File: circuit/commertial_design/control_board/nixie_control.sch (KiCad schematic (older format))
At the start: 34 parts, among them IC1 ATMEGA328P-A, P1 CONN_01X08, P2 CONN_02X03, P3 CONN_01X12, P4 CONN_01X04, P5 BLUETOOTH_SJ, P6 CONN_02X03, Q3 Q_NPN_EBC, Q4 Q_NPN_EBC, SW1 SW_PUSH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

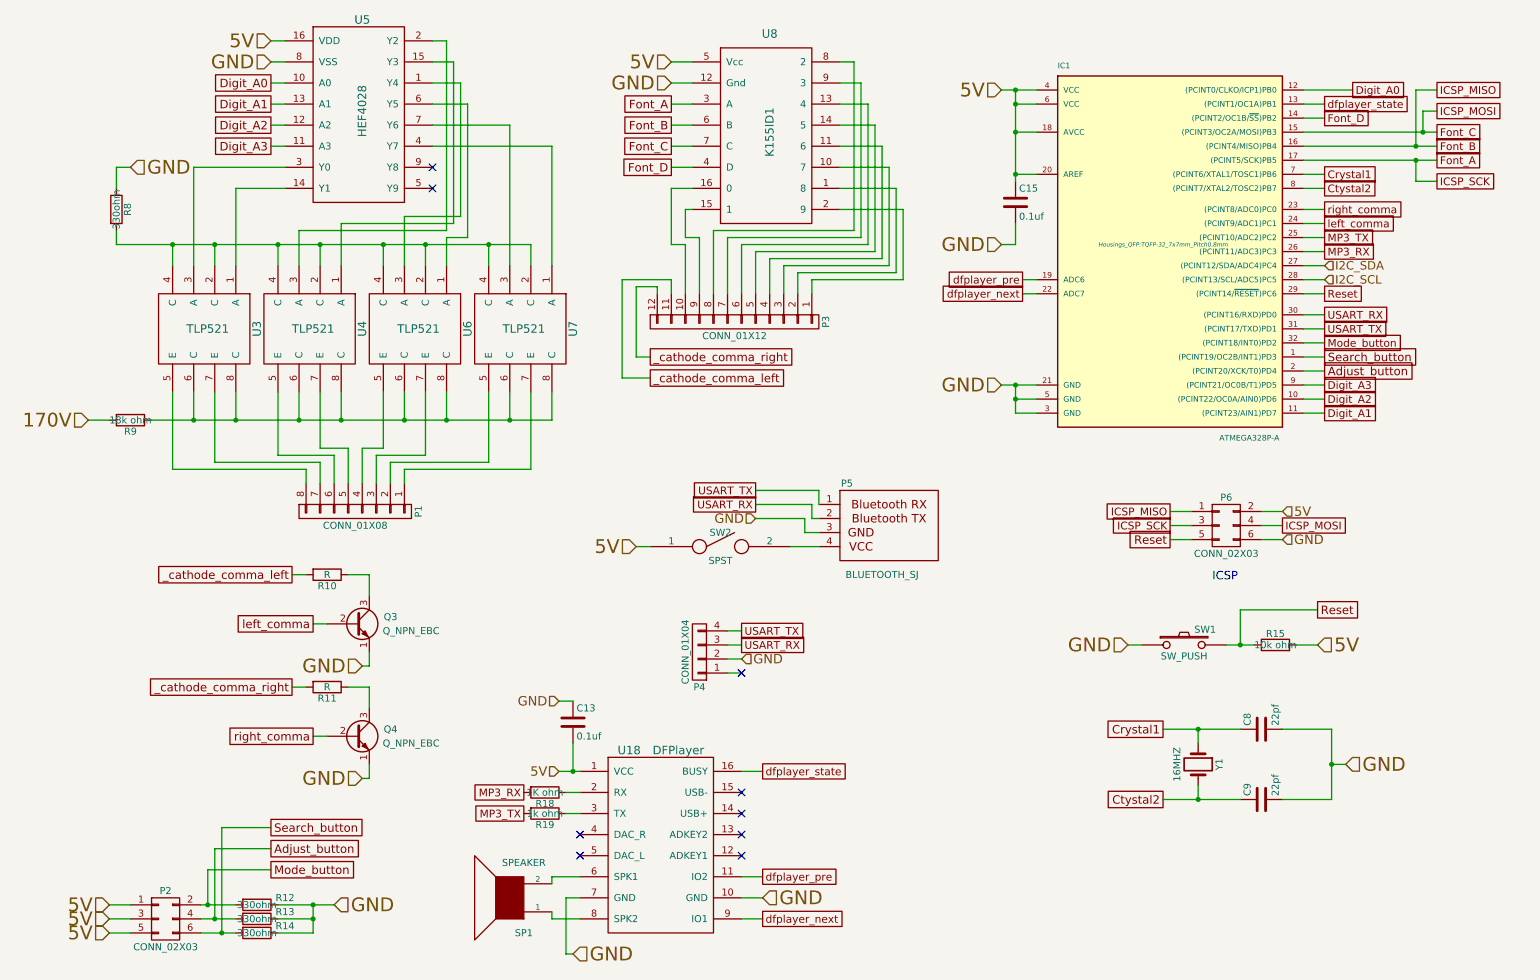
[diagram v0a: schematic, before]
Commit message: Layout need to be arranged, scheme is finished
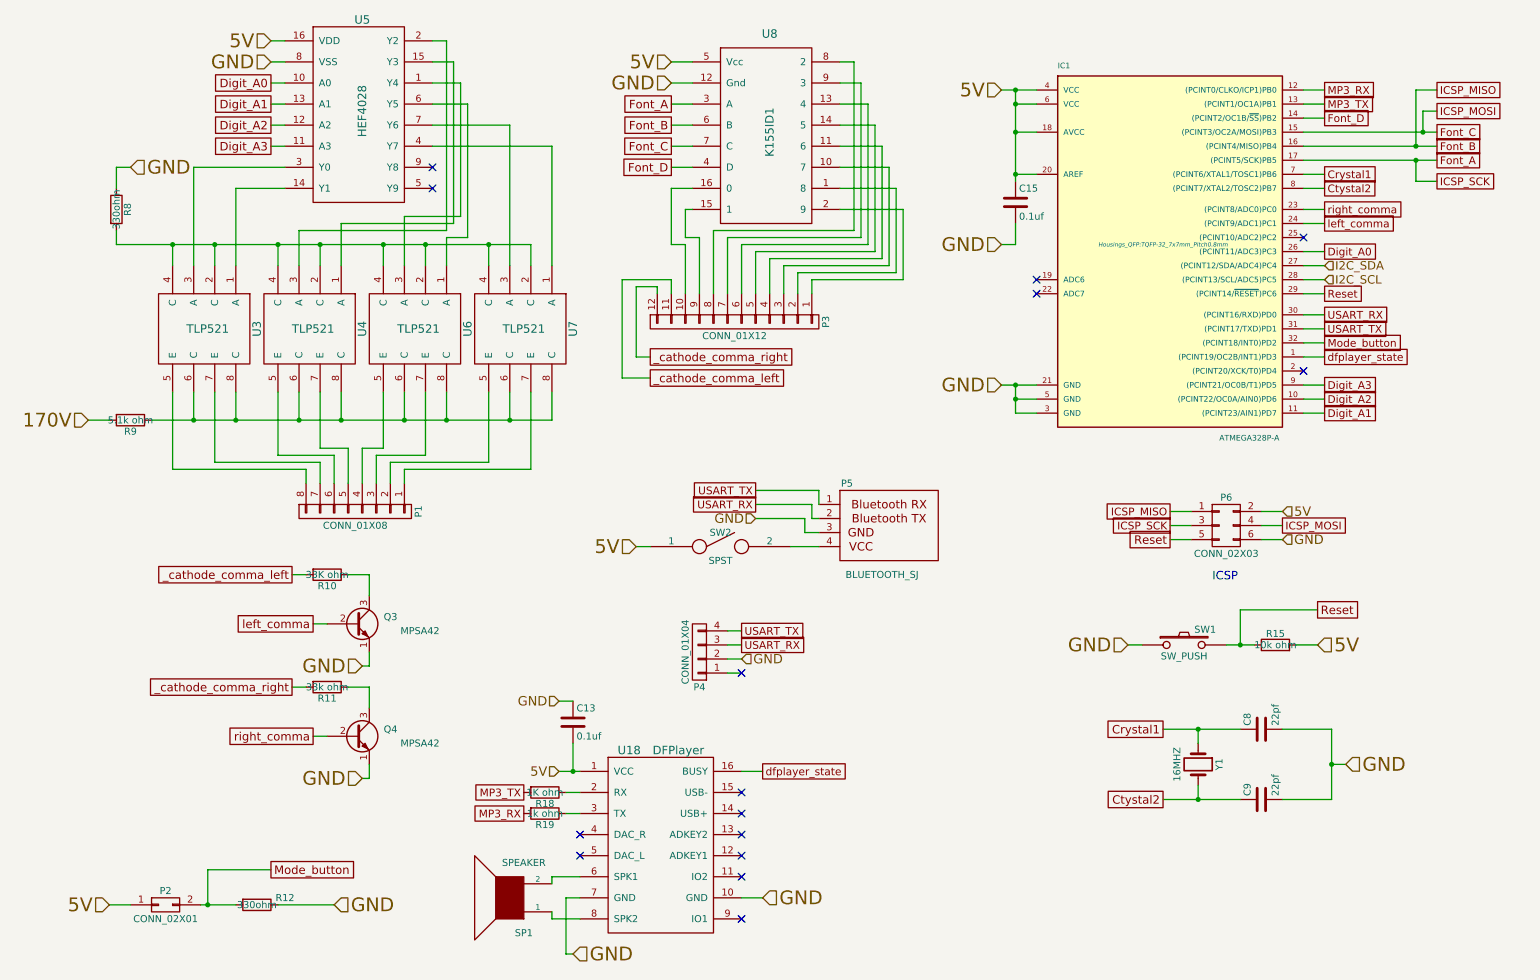
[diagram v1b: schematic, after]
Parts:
- removed P2: CONN_02X03, SMD_PIN_2_BY_3_REVERSE:SMD_PIN_2_BY_3_REVERSE, symbol CONN_02X03
- removed R13, R14: 330ohm, Resistors_SMD:R_1206_HandSoldering, symbol R
- added P2: CONN_02X01, Pin_Headers:Pin_Header_Straight_2x01, symbol CONN_02X01
- Q3, Q4: value Q_NPN_EBC -> MPSA42
- R10: value R -> 33K ohm
- R11: value R -> 33k ohm
- R9: value 18k ohm -> 5.1k ohm
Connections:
- net Search_button is gone; now on net dfplayer_state: IC1.1 ((PCINT19/OC2B/INT1)PD3)
- net 5V: now also P2.1 (P1)
- net Digit_A0: now also IC1.26 ((PCINT11/ADC3)PC3); no longer IC1.12 ((PCINT0/CLKO/ICP1)PB0)
- net MP3_RX: now also IC1.12 ((PCINT0/CLKO/ICP1)PB0), R19.2; no longer IC1.26 ((PCINT11/ADC3)PC3), R18.2
- net MP3_TX: now also IC1.13 ((PCINT1/OC1A)PB1), R18.2; no longer IC1.25 ((PCINT10/ADC2)PC2), R19.2
- net Mode_button: now also P2.2 (P2)
- net dfplayer_state: no longer IC1.13 ((PCINT1/OC1A)PB1)
- net Adjust_button: no longer names the net of IC1.2 ((PCINT20/XCK/T0)PD4)
- net dfplayer_next: no longer names the net of IC1.22 (ADC7)
- net dfplayer_next: no longer U18.9 (IO1)
- net dfplayer_pre: no longer names the net of IC1.19 (ADC6)
- net dfplayer_pre: no longer U18.11 (IO2)
- no-connect marks 9 -> 15
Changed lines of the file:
@@
 P 1400 3600
 F 0 "R9" V 1480 3600 50  0000 C CNN
-F 1 "18k ohm" V 1400 3600 50  0000 C CNN
+F 1 "5.1k ohm" V 1400 3600 50  0000 C CNN
 F 2 "Resistors_SMD:R_1206_HandSoldering" V 1330 3600 30  0001 C CNN
 F 3 "" H 1400 3600 30  0000 C CNN
@@
 Text GLabel 5250 1800 0    60   UnSpc ~ 0
 Font_D
-Text GLabel 10100 1250 2    55   UnSpc ~ 0
+Text GLabel 9900 2400 2    55   UnSpc ~ 0
 Digit_A0
 Text GLabel 9900 3550 2    55   UnSpc ~ 0
@@
 P 3000 5050
 F 0 "Q3" H 3300 5100 50  0000 R CNN
-F 1 "Q_NPN_EBC" H 3600 5000 50  0000 R CNN
+F 1 "MPSA42" H 3600 5000 50  0000 R CNN
 F 2 "TO_SOT_Packages_THT:TO-92_Inline_Narrow_Oval" H 3200 5150 29  0001 C CNN
 F 3 "" H 3000 5050 60  0000 C CNN
@@
 P 3000 5850
 F 0 "Q4" H 3300 5900 50  0000 R CNN
-F 1 "Q_NPN_EBC" H 3600 5800 50  0000 R CNN
+F 1 "MPSA42" H 3600 5800 50  0000 R CNN
 F 2 "TO_SOT_Packages_THT:TO-92_Inline_Narrow_Oval" H 3200 5950 29  0001 C CNN
 F 3 "" H 3000 5850 60  0000 C CNN
@@
 P 2800 4700
 F 0 "R10" V 2880 4700 50  0000 C CNN
-F 1 "R" V 2800 4700 50  0000 C CNN
+F 1 "33K ohm" V 2800 4700 50  0000 C CNN
 F 2 "Resistors_SMD:R_1206_HandSoldering" V 2730 4700 30  0001 C CNN
 F 3 "" H 2800 4700 30  0000 C CNN
@@
 P 2800 5500
 F 0 "R11" V 2880 5500 50  0000 C CNN
-F 1 "R" V 2800 5500 50  0000 C CNN
+F 1 "33k ohm" V 2800 5500 50  0000 C CNN
 F 2 "Resistors_SMD:R_1206_HandSoldering" V 2730 5500 30  0001 C CNN
 F 3 "" H 2800 5500 30  0000 C CNN
@@
 _cathode_comma_left
 $Comp
-L CONN_02X03 P2
-U 1 1 56A879D5
-P 1650 7150
-F 0 "P2" H 1650 7350 50  0000 C CNN
-F 1 "CONN_02X03" H 1650 6950 50  0000 C CNN
-F 2 "SMD_PIN_2_BY_3_REVERSE:SMD_PIN_2_BY_3_REVERSE" H 1650 5950 50  0001 C CNN
-F 3 "" H 1650 5950 50  0000 C CNN
-	1    1650 7150
-	1    0    0    -1
-$EndComp
-Text HLabel 1250 7150 0    98   Input ~ 0
-5V
-Text HLabel 1250 7250 0    98   Input ~ 0
-5V
-$Comp
-L R R13
-U 1 1 56A87DD8
-P 2300 7150
-F 0 "R13" V 2250 7350 50  0000 C CNN
-F 1 "330ohm" V 2300 7150 50  0000 C CNN
-F 2 "Resistors_SMD:R_1206_HandSoldering" V 2230 7150 30  0001 C CNN
-F 3 "" H 2300 7150 30  0000 C CNN
-	1    2300 7150
-	0    1    1    0
-$EndComp
-$Comp
-L R R14
-U 1 1 56A87E33
-P 2300 7250
-F 0 "R14" V 2250 7450 50  0000 C CNN
-F 1 "330ohm" V 2300 7250 50  0000 C CNN
-F 2 "Resistors_SMD:R_1206_HandSoldering" V 2230 7250 30  0001 C CNN
-F 3 "" H 2300 7250 30  0000 C CNN
-	1    2300 7250
-	0    1    1    0
-$EndComp
-Text GLabel 2400 6650 2    60   UnSpc ~ 0
-Adjust_button
-Text GLabel 2400 6500 2    60   UnSpc ~ 0
-Search_button
-Text GLabel 9900 3250 2    60   UnSpc ~ 0
-Adjust_button
-Text GLabel 9900 3150 2    60   UnSpc ~ 0
-Search_button
-$Comp
 L R R18
 U 1 1 56ACF8C9
@@
 Text HLabel 4450 6100 0    67   Input ~ 0
 5V
-Text GLabel 9900 2300 2    55   UnSpc ~ 0
+Text GLabel 9900 1350 2    55   UnSpc ~ 0
 MP3_TX
-Text GLabel 9900 2400 2    55   UnSpc ~ 0
+Text GLabel 9900 1250 2    55   UnSpc ~ 0
 MP3_RX
+Text GLabel 4200 6250 0    55   UnSpc ~ 0
+MP3_TX
 Text GLabel 4200 6400 0    55   UnSpc ~ 0
-MP3_TX
-Text GLabel 4200 6250 0    55   UnSpc ~ 0
 MP3_RX
 $Comp
@@
 	1    0    0    -1
 $EndComp
-Text GLabel 9900 1350 2    55   UnSpc ~ 0
+Text GLabel 9900 3150 2    55   UnSpc ~ 0
 dfplayer_state
 Text GLabel 5900 6100 2    55   UnSpc ~ 0
@@
 Text HLabel 5900 7000 2    98   Input ~ 0
 GND
-Text GLabel 7750 2600 0    55   UnSpc ~ 0
-dfplayer_pre
-Text GLabel 7750 2700 0    55   UnSpc ~ 0
-dfplayer_next
-Text GLabel 5900 6850 2    55   UnSpc ~ 0
-dfplayer_pre
-Text GLabel 5900 7150 2    55   UnSpc ~ 0
-dfplayer_next
 $Comp
 L C C15
@@
 Connection ~ 7700 1850
 Wire Wire Line
-	5750 7150 5900 7150
-Wire Wire Line
-	5750 6850 5900 6850
-Wire Wire Line
-	7750 2700 7850 2700
-Wire Wire Line
-	7750 2600 7850 2600
-Wire Wire Line
 	5750 7000 5900 7000
 Wire Wire Line
@@
 	4500 6250 4600 6250
 Wire Wire Line
-	9750 3250 9900 3250
-Wire Wire Line
 	9750 3150 9900 3150
-Connection ~ 2050 7250
-Wire Wire Line
-	2050 6500 2400 6500
-Wire Wire Line
-	2050 7250 2050 6500
-Connection ~ 2000 7150
-Wire Wire Line
-	2000 6650 2000 7150
-Wire Wire Line
-	2400 6650 2000 6650
-Connection ~ 2700 7150
-Wire Wire Line
-	2700 7250 2450 7250
-Connection ~ 2700 7050
-Wire Wire Line
-	2700 7050 2700 7250
-Wire Wire Line
-	2450 7150 2700 7150
-Wire Wire Line
-	1900 7250 2150 7250
-Wire Wire Line
-	1900 7150 2150 7150
-Wire Wire Line
-	1400 7250 1250 7250
-Wire Wire Line
-	1250 7150 1400 7150
 Wire Wire Line
 	7700 1250 7700 1900
@@
 Wire Wire Line
 	9900 2400 9750 2400
-Wire Wire Line
-	9750 2300 9900 2300
 Wire Wire Line
 	2550 5500 2650 5500
@@
 Wire Wire Line
 	9750 1450 9900 1450
-Wire Wire Line
-	9750 1250 10100 1250
 Wire Wire Line
 	5350 2100 5350 2300
@@
 Wire Wire Line
 	8800 4250 8950 4250
+Wire Wire Line
+	9750 1250 9900 1250
+$Comp
+L CONN_02X01 P2
+U 1 1 57A4962D
+P 1650 7050
+F 0 "P2" H 1650 7150 50  0000 C CNN
+F 1 "CONN_02X01" H 1650 6950 50  0000 C CNN
+F 2 "Pin_Headers:Pin_Header_Straight_2x01" H 1650 5850 50  0001 C CNN
+F 3 "" H 1650 5850 50  0000 C CNN
+	1    1650 7050
+	1    0    0    -1
+$EndComp
+NoConn ~ 5750 6850
+NoConn ~ 5750 7150
+NoConn ~ 9750 3250
+NoConn ~ 9750 2300
+NoConn ~ 7850 2600
+NoConn ~ 7850 2700
 $EndSCHEMATC

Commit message: Update commertial board
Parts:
- P1: footprint SMD_PIN_2_BY_4_REVERSE:SMD_PIN_2_BY_4_REVERSE -> Pin_Headers:Pin_Header_Straight_2x04
- P3: footprint SMD_PIN_2_BY_6_REVERSE:SMD_PIN_2_BY_6_REVERSE -> Pin_Headers:Pin_Header_Straight_2x06
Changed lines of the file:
@@
 F 0 "P1" H 3000 4700 50  0000 C CNN
 F 1 "CONN_01X08" V 3100 4250 50  0000 C CNN
-F 2 "SMD_PIN_2_BY_4_REVERSE:SMD_PIN_2_BY_4_REVERSE" H 3000 4250 50  0001 C CNN
+F 2 "Pin_Headers:Pin_Header_Straight_2x04" H 3000 4250 50  0001 C CNN
 F 3 "" H 3000 4250 50  0000 C CNN
 	1    3000 4250
@@
 F 0 "P3" H 5700 3550 50  0000 C CNN
 F 1 "CONN_01X12" V 5800 2900 50  0000 C CNN
-F 2 "SMD_PIN_2_BY_6_REVERSE:SMD_PIN_2_BY_6_REVERSE" H 5700 2900 50  0001 C CNN
+F 2 "Pin_Headers:Pin_Header_Straight_2x06" H 5700 2900 50  0001 C CNN
 F 3 "" H 5700 2900 50  0000 C CNN
 	1    5700 2900

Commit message: Fix PCB board
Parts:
- U8: value K155ID1 -> 74L147
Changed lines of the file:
@@
 P 5950 1600
 F 0 "U8" H 5950 2350 60  0000 C CNN
-F 1 "K155ID1" V 5950 1650 60  0000 C CNN
+F 1 "74L147" V 5950 1650 60  0000 C CNN
 F 2 "Housings_DIP:DIP-16_W7.62mm" H 5950 2350 60  0001 C CNN
 F 3 "" H 5950 2350 60  0000 C CNN

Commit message: Fix board errors
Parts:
- removed P5: BLUETOOTH_SJ, HC06:HC06, symbol BLUETOOTH_SJ
- removed SW2: SPST, SMD_SOLD_BRIDGE:SMD_BRIDGE, symbol SPST
- added U11: hc06, hc06:hc06, symbol hc06
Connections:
- net GND: now also U11.13 (GND), U11.22 (GND)
- net USART_RX: now also U11.1 (TX)
- net USART_TX: now also U11.2 (RX)
- new net 3V3: U11.12 (3.3V)
- no-connect marks 15 -> 44
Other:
- moved on the sheet: P4
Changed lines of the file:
@@
 LIBS:valves
 LIBS:costom
+LIBS:hc06
 LIBS:nixie_control_board-cache
 EELAYER 25 0
@@
 $Descr A4 11693 8268
 encoding utf-8
-Sheet 3 4
+Sheet 2 4
 Title ""
 Date ""
@@
 Text GLabel 9900 2950 2    55   UnSpc ~ 0
 USART_TX
-Text HLabel 5850 4300 0    67   Input ~ 0
-GND
-Text HLabel 5750 5300 2    67   Input ~ 0
-GND
-Text GLabel 5850 4200 0    55   UnSpc ~ 0
+Text HLabel 7150 4500 2    67   Input ~ 0
+GND
+Text GLabel 4850 3900 0    55   UnSpc ~ 0
 USART_RX
-Text GLabel 5850 4100 0    55   UnSpc ~ 0
+Text GLabel 4850 4000 0    55   UnSpc ~ 0
 USART_TX
-Text GLabel 5750 5200 2    55   UnSpc ~ 0
+Text GLabel 7150 4400 2    55   UnSpc ~ 0
 USART_RX
-Text GLabel 5750 5100 2    55   UnSpc ~ 0
+Text GLabel 7150 4300 2    55   UnSpc ~ 0
 USART_TX
 Text GLabel 9900 3050 2    55   UnSpc ~ 0
@@
 L CONN_01X04 P4
 U 1 1 57408260
-P 5450 5250
-F 0 "P4" H 5450 5500 50  0000 C CNN
-F 1 "CONN_01X04" V 5550 5250 50  0000 C CNN
-F 2 "Pin_Headers:Pin_Header_Straight_1x04" H 5450 5250 50  0001 C CNN
-F 3 "" H 5450 5250 50  0000 C CNN
-	1    5450 5250
+P 6850 4450
+F 0 "P4" H 6850 4700 50  0000 C CNN
+F 1 "CONN_01X04" V 6950 4450 50  0000 C CNN
+F 2 "Pin_Headers:Pin_Header_Straight_1x04" H 6850 4450 50  0001 C CNN
+F 3 "" H 6850 4450 50  0000 C CNN
+	1    6850 4450
 	-1   0    0    1
-$EndComp
-$Comp
-L SPST SW2
-U 1 1 57408470
-P 5600 4500
-F 0 "SW2" H 5600 4600 50  0000 C CNN
-F 1 "SPST" H 5600 4400 50  0000 C CNN
-F 2 "SMD_SOLD_BRIDGE:SMD_BRIDGE" H 5600 4500 50  0001 C CNN
-F 3 "" H 5600 4500 50  0000 C CNN
-	1    5600 4500
-	1    0    0    -1
-$EndComp
-$Comp
-L BLUETOOTH_SJ P5
-U 1 1 574BA9A7
-P 6500 4350
-F 0 "P5" H 6500 4650 50  0000 C CNN
-F 1 "BLUETOOTH_SJ" H 6750 4000 50  0000 C CNN
-F 2 "HC06:HC06" H 6550 4350 50  0001 C CNN
-F 3 "" H 6550 4350 50  0000 C CNN
-	1    6500 4350
-	1    0    0    -1
 $EndComp
 Text GLabel 9900 3150 2    55   UnSpc ~ 0
@@
 Text HLabel 7600 2350 0    98   Input ~ 0
 GND
-Text HLabel 5000 4500 0    98   Input ~ 0
-5V
 $Comp
 L C C13
@@
 Text HLabel 4450 5600 0    67   Input ~ 0
 GND
-NoConn ~ 5750 5400
+NoConn ~ 7150 4600
 $Comp
 L CONN_02X03 P6
@@
 	9750 1350 9900 1350
 Wire Wire Line
-	6300 4100 6300 4200
-Wire Wire Line
-	6250 4300 6300 4300
-Wire Wire Line
-	6250 4200 6250 4300
-Wire Wire Line
-	6200 4400 6300 4400
-Wire Wire Line
-	6200 4300 6200 4400
-Wire Wire Line
-	6100 4500 6300 4500
-Wire Wire Line
 	7700 1850 7850 1850
 Wire Wire Line
@@
 	9900 3050 9750 3050
 Wire Wire Line
-	5000 4500 5100 4500
-Wire Wire Line
-	5750 5400 5650 5400
-Wire Wire Line
-	5750 5200 5650 5200
-Wire Wire Line
-	5650 5100 5750 5100
-Wire Wire Line
-	5850 4200 6250 4200
-Wire Wire Line
-	5850 4100 6300 4100
-Wire Wire Line
-	5650 5300 5750 5300
-Wire Wire Line
-	5850 4300 6200 4300
+	7150 4600 7050 4600
+Wire Wire Line
+	7150 4400 7050 4400
+Wire Wire Line
+	7050 4300 7150 4300
+Wire Wire Line
+	7050 4500 7150 4500
 Wire Wire Line
 	9750 2950 9900 2950
@@
 NoConn ~ 7850 2600
 NoConn ~ 7850 2700
+NoConn ~ 6300 3900
+NoConn ~ 6300 4000
+NoConn ~ 6300 4100
+NoConn ~ 6300 4200
+NoConn ~ 6300 4300
+NoConn ~ 6300 4400
+NoConn ~ 6300 4500
+NoConn ~ 6300 4600
+NoConn ~ 6300 4700
+NoConn ~ 6300 4800
+NoConn ~ 6300 4900
+NoConn ~ 6300 5000
+NoConn ~ 5950 5550
+NoConn ~ 5850 5550
+NoConn ~ 5750 5550
+NoConn ~ 5650 5550
+NoConn ~ 5550 5550
+NoConn ~ 5450 5550
+NoConn ~ 5350 5550
+NoConn ~ 5250 5550
+NoConn ~ 4900 4100
+NoConn ~ 4900 4200
+NoConn ~ 4900 4300
+NoConn ~ 4900 4400
+NoConn ~ 4900 4500
+NoConn ~ 4900 4600
+NoConn ~ 4900 4700
+NoConn ~ 4900 4800
+NoConn ~ 4900 4900
+Text HLabel 6450 5100 2    98   Input ~ 0
+GND
+Wire Wire Line
+	6300 5100 6450 5100
+Text HLabel 4750 5150 0    98   Input ~ 0
+GND
+Wire Wire Line
+	4800 5150 4800 5100
+Wire Wire Line
+	4800 5100 4900 5100
+Wire Wire Line
+	4750 5150 4800 5150
+Wire Wire Line
+	4850 3900 4900 3900
+Wire Wire Line
+	4900 4000 4850 4000
+$Comp
+L hc06 U11
+U 1 1 58930ADF
+P 5600 4450
+F 0 "U11" H 6000 5250 60  0000 C CNN
+F 1 "hc06" H 5200 5250 60  0000 C CNN
+F 2 "hc06:hc06" H 5300 5150 60  0001 C CNN
+F 3 "" H 5300 5150 60  0001 C CNN
+	1    5600 4450
+	1    0    0    -1
+$EndComp
+Wire Wire Line
+	4750 5000 4900 5000
+Text HLabel 4750 5000 0    98   Input ~ 0
+3V3
 $EndSCHEMATC
